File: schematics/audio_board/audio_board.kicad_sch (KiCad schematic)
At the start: 52 parts, among them J1 servo ctrl, J10 charge en, J3 power, J4 pyr ctrl, J5 servo out, J6 pyr in, J7 audio ctrl, J8 speaker, J9 battery, U1 TPS613222ADBV, U3 TPS613222ADBV, U4 TPS613222ADBV, U5 PAM8302AAD, U8 MCP73812

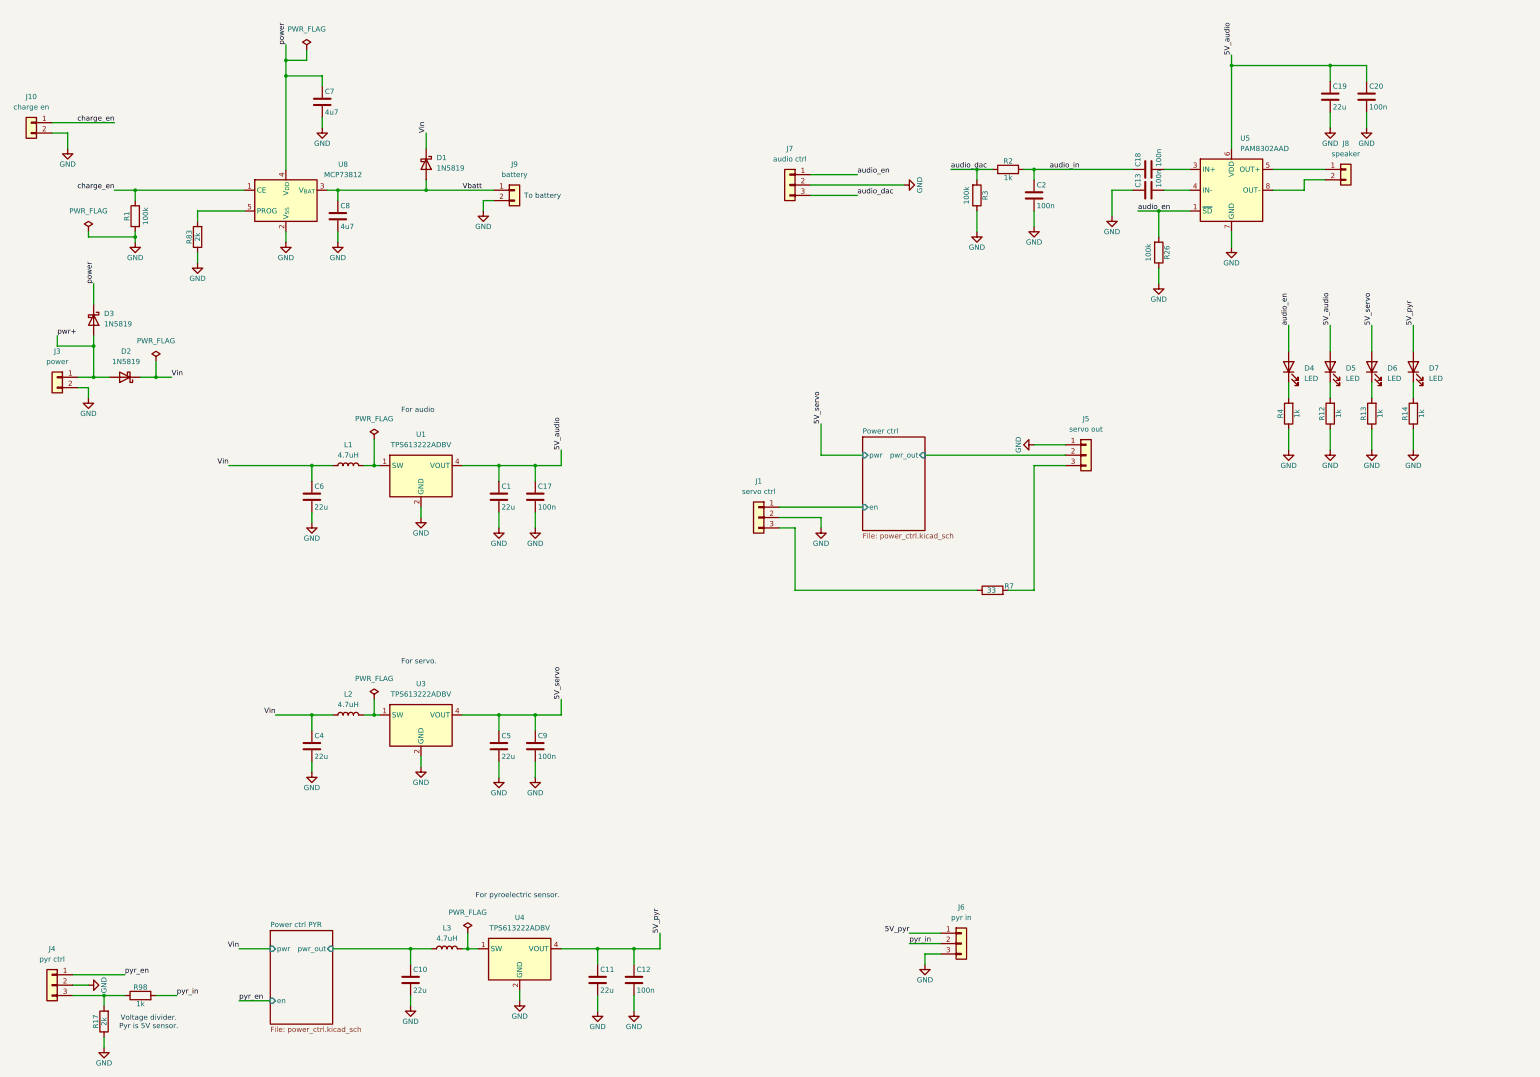
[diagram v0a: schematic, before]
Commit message: Redesigning audio board to support microphone.
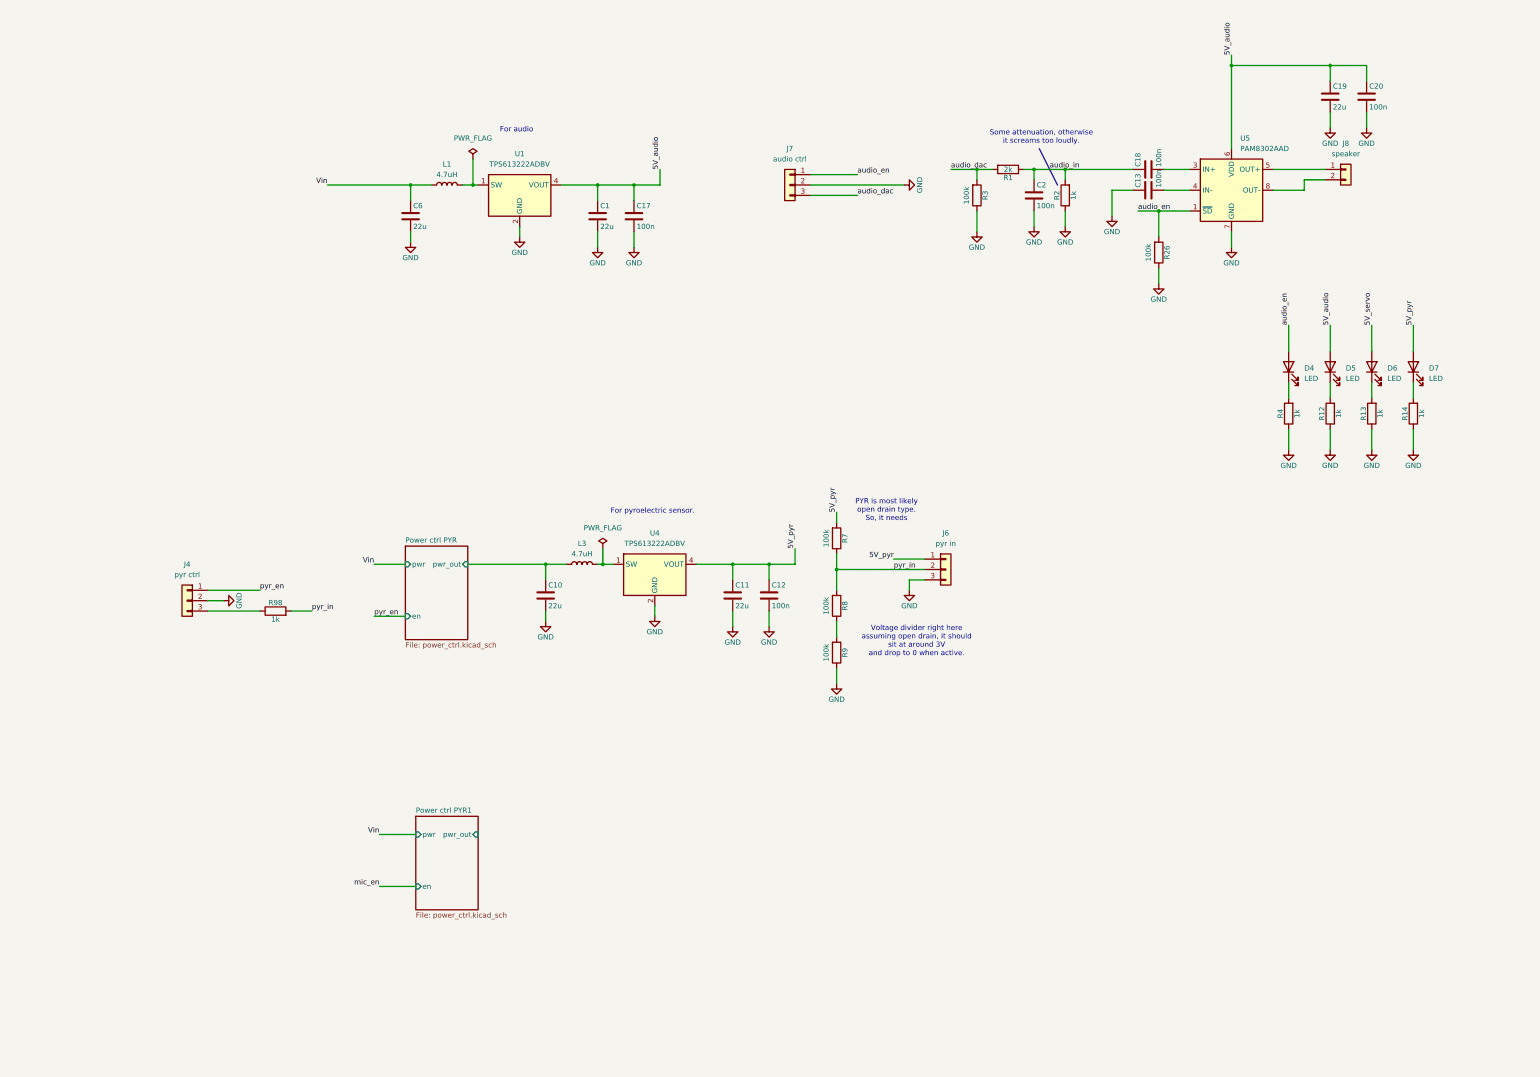
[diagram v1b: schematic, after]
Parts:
- removed C4, C5: 22u, Capacitor_SMD:C_0603_1608Metric_Pad1.08x0.95mm_HandSolder, symbol Device:C
- removed C7, C8: 4u7, Capacitor_SMD:C_0603_1608Metric_Pad1.08x0.95mm_HandSolder, symbol Device:C
- removed C9: 100n, Capacitor_SMD:C_0603_1608Metric_Pad1.08x0.95mm_HandSolder, symbol Device:C
- removed D1, D2, D3: 1N5819, Diode_THT:D_DO-41_SOD81_P7.62mm_Horizontal, symbol Device:D_Schottky
- removed J1: servo ctrl, Connector_PinSocket_2.54mm:PinSocket_1x03_P2.54mm_Vertical, symbol Connector_Generic:Conn_01x03
- removed J10: charge en, Connector_PinSocket_2.54mm:PinSocket_1x02_P2.54mm_Vertical, symbol Connector_Generic:Conn_01x02
- removed J3: power, Connector_PinSocket_2.54mm:PinSocket_1x02_P2.54mm_Vertical, symbol Connector_Generic:Conn_01x02
- removed J5: servo out, Connector_PinSocket_2.54mm:PinSocket_1x03_P2.54mm_Vertical, symbol Connector_Generic:Conn_01x03
- removed J9: battery, Connector_PinSocket_2.54mm:PinSocket_1x02_P2.54mm_Vertical, symbol Connector_Generic:Conn_01x02
- removed L2: 4.7uH, Inductor_SMD:L_1008_2520Metric, symbol Device:L
- removed R17, R83: 2k, Capacitor_SMD:C_0603_1608Metric_Pad1.08x0.95mm_HandSolder, symbol Device:R
- removed U3: TPS613222ADBV, Package_TO_SOT_SMD:SOT-23-5, symbol Regulator_Switching:TPS613222ADBV
- removed U8: MCP73812, Package_TO_SOT_SMD:SOT-23-5, symbol Battery_Management:MCP73812T-420I-OT
- added R8, R9: 100k, Resistor_SMD:R_0603_1608Metric_Pad0.98x0.95mm_HandSolder, symbol Device:R
- R1: value 100k -> 2k; footprint Resistor_SMD:R_0603_1608Metric_Pad0.98x0.95mm_HandSolder -> Capacitor_SMD:C_0603_1608Metric_Pad1.08x0.95mm_HandSolder; URL (none) -> https://www.digikey.com/en/products/detail/yageo/AC0603JR-0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
- R7: value 33 -> 100k
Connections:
- net charge_en is gone; now on net audio_in: R1.1
- net 5V_pyr: now also R7.2
- net GND: now also R2.1, R9.1; no longer R1.2
- net audio_dac: now also R1.2; no longer R2.1
- net pyr_in: now also R7.1, R8.2
- new net: R8.1, R9.2
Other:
- removed sheet Power ctrl
- added sheet Power ctrl PYR1 (power_ctrl.kicad_sch)
- note added: "PYR is most likely open drain type. So, it needs"
- note added: "Some attenuation, otherwise it screams too loudly."
- note added: "Voltage divider right here assuming open drain, it should sit at around 3V and drop to 0 when active."
- note removed: "For servo."
- note removed: "To battery"
- note removed: "Voltage divider. Pyr is 5V sensor."
- moved on the sheet: C1, C10, C11, C12, C17, C6, J4, J6, L1, L3, R2, R98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

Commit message: Replaced thick film with thin film resistors in feedback loops.
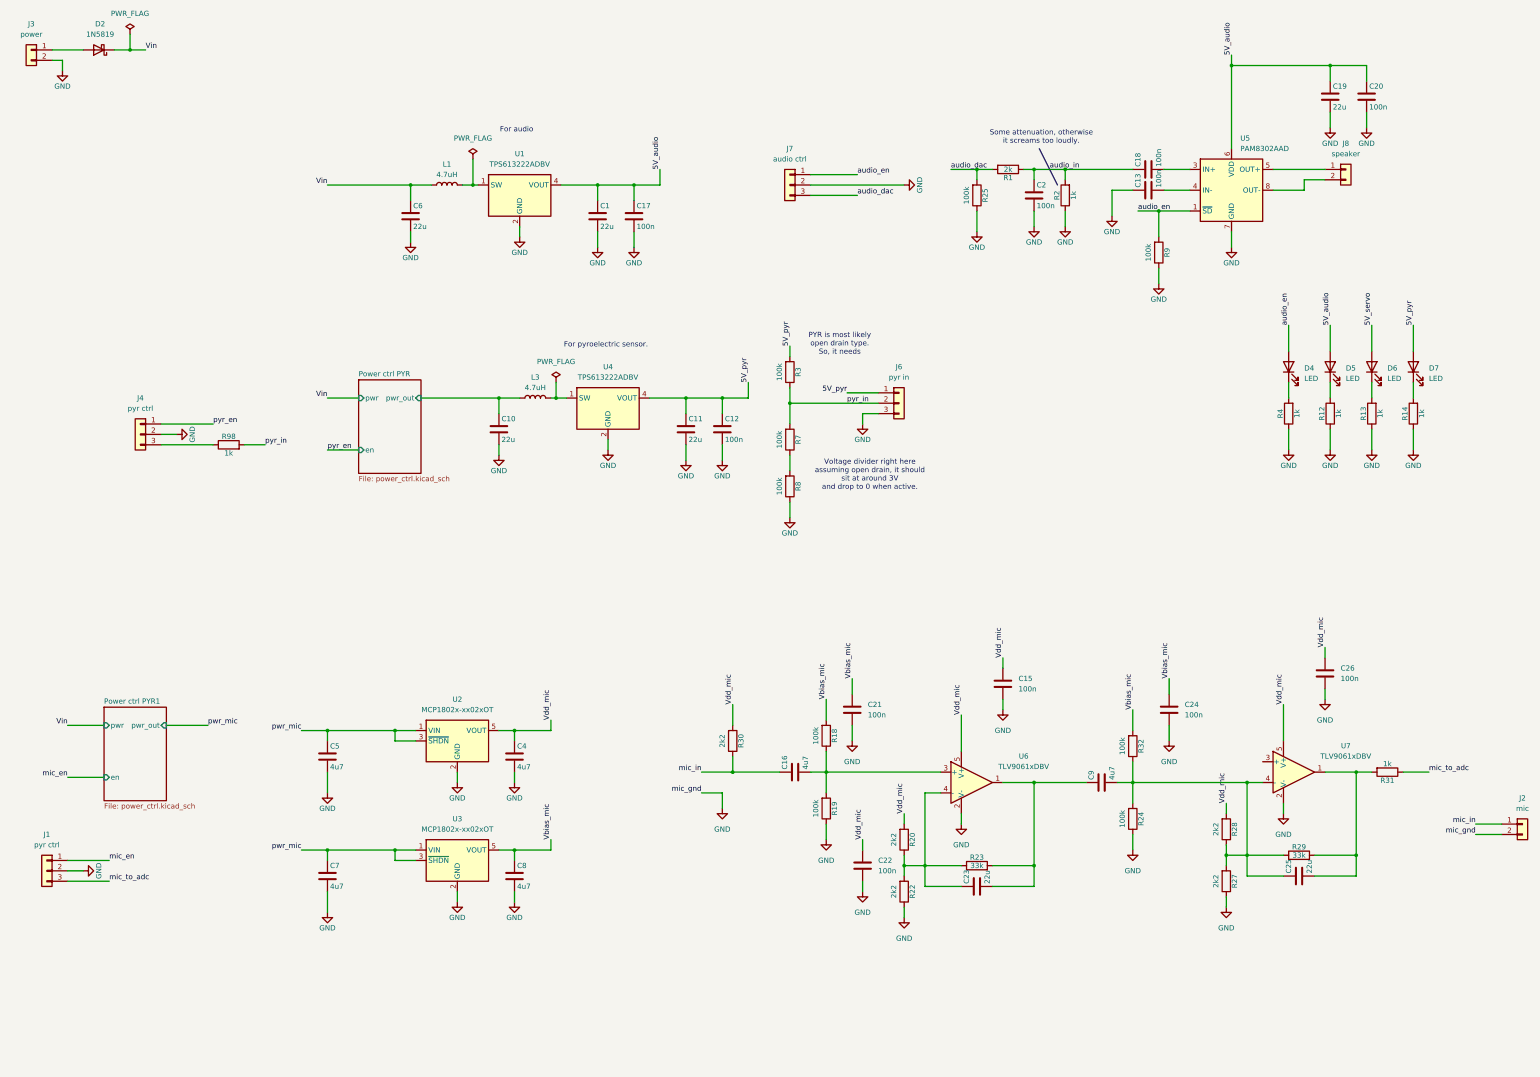
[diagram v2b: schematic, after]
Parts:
- removed R26: 100k, Resistor_SMD:R_0603_1608Metric_Pad0.98x0.95mm_HandSolder, symbol Device:R
- added C15, C21, C22, C24, C26: 100n, Capacitor_SMD:C_0603_1608Metric, symbol Device:C
- added C16, C4, C5, C7, C8, C9: 4u7, Capacitor_SMD:C_0603_1608Metric, symbol Device:C
- added C23, C25: 22u, Capacitor_SMD:C_0603_1608Metric_Pad1.08x0.95mm_HandSolder, symbol Device:C
- added D2: 1N5819, Diode_THT:D_DO-41_SOD81_P7.62mm_Horizontal, symbol Device:D_Schottky
- added J1: pyr ctrl, Connector_PinSocket_2.54mm:PinSocket_1x03_P2.54mm_Vertical, symbol Connector_Generic:Conn_01x03
- added J2: mic, Connector_PinSocket_2.54mm:PinSocket_1x02_P2.54mm_Vertical, symbol Connector_Generic:Conn_01x02
- added J3: power, Connector_PinSocket_2.54mm:PinSocket_1x02_P2.54mm_Vertical, symbol Connector_Generic:Conn_01x02
- added R18, R19, R24, R25, R32: 100k, Resistor_SMD:R_0603_1608Metric_Pad0.98x0.95mm_HandSolder, symbol Device:R
- added R20, R22, R27, R28, R30: 2k2, Resistor_SMD:R_0603_1608Metric_Pad0.98x0.95mm_HandSolder, symbol Device:R
- added R23, R29: 33k, Capacitor_SMD:C_0603_1608Metric_Pad1.08x0.95mm_HandSolder, symbol Device:R
- added R31: 1k, Capacitor_SMD:C_0603_1608Metric_Pad1.08x0.95mm_HandSolder, symbol Device:R
- added U2, U3: MCP1802x-xx02xOT, Package_TO_SOT_SMD:SOT-23-5, symbol Regulator_Linear:MCP1802x-xx02xOT
- added U6, U7: TLV9061xDBV, Package_TO_SOT_SMD:SOT-23-5, symbol Amplifier_Operational:TLV9061xDBV
- R3, R7, R8, R9: url (none) -> https://www.digikey.com/en/products/detail/susumu/RG1608P-1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
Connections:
- net 5V_pyr: now also R3.2; no longer R7.2
- net GND: now also R8.1, C15.2, C21.2, C22.2, C24.2, C26.2, C4.2, C5.2, C7.2, C8.2, J1.2 (Pin_2), J2.2 (Pin_2), J3.2 (Pin_2), R19.1, R22.1, R24.1, R25.1, R27.1, U2.2 (GND), U3.2 (GND), U6.2 (V-), U7.2 (V-); no longer R3.1
- net Vin: now also D2.1 (K)
- net audio_dac: now also R25.2; no longer R3.2
- net audio_en: now also R9.2
- net mic_en: now also J1.1 (Pin_1)
- net pyr_in: now also R3.1, R7.2; no longer R7.1, R8.2
- new net: R7.1, R8.2
- new net: C25.2, R29.2, R31.2, U7.1
- new net: C23.2, C9.1, R23.2, U6.1
- new net: C16.2, R18.1, R19.2, U6.3 (+)
- new net: C23.1, R20.1, R22.2, R23.1, U6.4 (-)
- new net: C25.1, C9.2, R24.2, R27.2, R28.1, R29.1, R32.1, U7.4 (-)
- new net: D2.2 (A), J3.1 (Pin_1)
- new net Vbias_mic: C21.1, C24.1, C8.1, R18.2, R32.2, U3.5 (VOUT)
- new net Vdd_mic: C15.1, C22.1, C26.1, C4.1, R20.2, R28.2, R30.2, U2.5 (VOUT), U6.5 (V+), U7.5 (V+)
- new net mic_in: C16.1, J2.1 (Pin_1), R30.1
- new net mic_to_adc: J1.3 (Pin_3), R31.1
- new net pwr_mic: C5.1, C7.1, U2.1 (VIN), U2.3 (~{SHDN}), U3.1 (VIN), U3.3 (~{SHDN})
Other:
- moved on the sheet: C10, C11, C12, J4, J6, L3, R98, U4

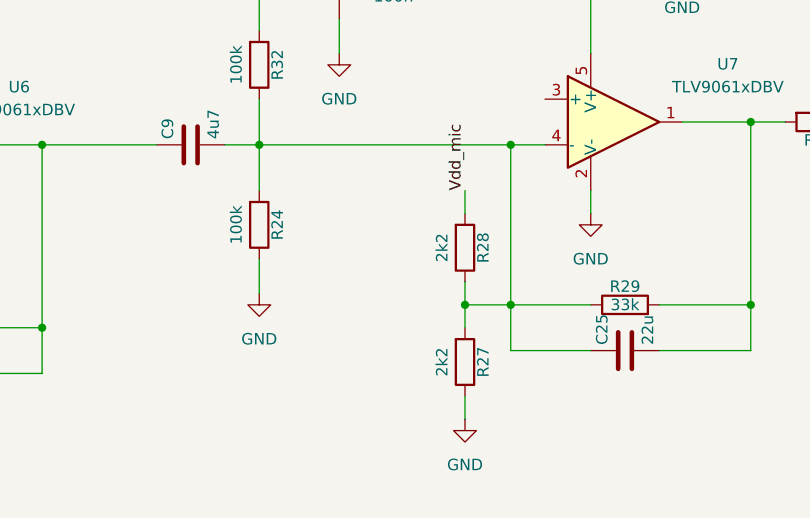
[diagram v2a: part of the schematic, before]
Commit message: Added filtering capacitor.
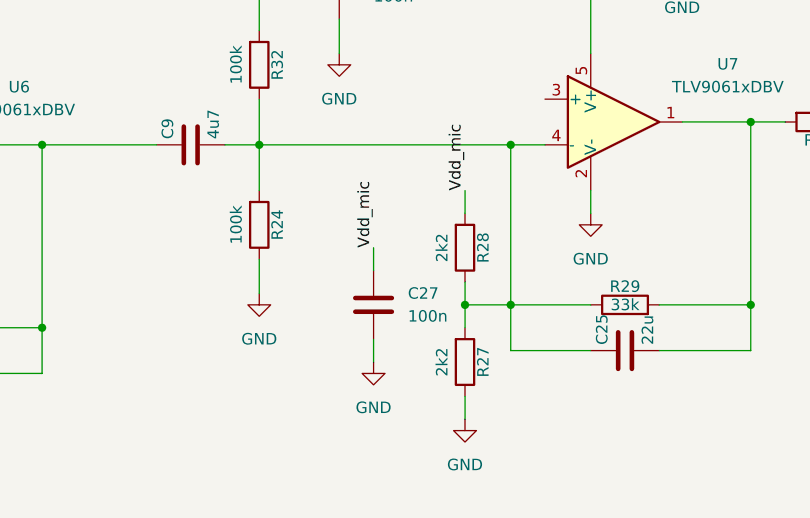
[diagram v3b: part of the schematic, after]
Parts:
- added C27: 100n, Capacitor_SMD:C_0603_1608Metric, symbol Device:C
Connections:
- net GND: now also C27.2
- net Vdd_mic: now also C27.1
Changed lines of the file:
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@@
 	(wire
 		(pts
+			(xy 306.07 214.63) (xy 306.07 217.17)
+		)
+		(stroke
+			(width 0)
+			(type default)
+		)
+	)
+	(wire
+		(pts
 			(xy 341.63 39.37) (xy 341.63 43.18)
 		)
@@
 	(wire
 		(pts
+			(xy 306.07 224.79) (xy 306.07 227.33)
+		)
+		(stroke
+			(width 0)
+			(type default)
+		)
+	)
+	(wire
+		(pts
 			(xy 289.56 203.2) (xy 293.37 203.2)
 		)
@@
 		)
 	)
+	(label "Vdd_mic"
+		(at 306.07 214.63 90)
+		(effects
+			(font
+				(size 1.27 1.27)
+			)
+			(justify left bottom)
+		)
+	)
 	(label "mic_in"
 		(at 187.96 200.66 180)
@@
 	(symbol
 		(lib_id "Device:C")
+		(at 306.07 220.98 0)
+		(unit 1)
+		(exclude_from_sim no)
+		(in_bom yes)
+		(on_board yes)
+		(dnp no)
+		(fields_autoplaced yes)
+		(property "Reference" "C27"
+			(at 309.88 219.7099 0)
+			(effects
+				(font
+					(size 1.27 1.27)
+				)
+				(justify left)
+			)
+		)
+		(property "Value" "100n"
+			(at 309.88 222.2499 0)
+			(effects
+				(font
+					(size 1.27 1.27)
+				)
+				(justify left)
+			)
+		)
+		(property "Footprint" "Capacitor_SMD:C_0603_1608Metric"
+			(at 307.0352 224.79 0)
+			(effects
+				(font
+					(size 1.27 1.27)
+				)
+				(hide yes)
+			)
+		)
+		(property "Datasheet" "~"
+			(at 306.07 220.98 0)
+			(effects
+				(font
+					(size 1.27 1.27)
+				)
+				(hide yes)
+			)
+		)
+		(property "Description" "Unpolarized capacitor"
+			(at 306.07 220.98 0)
+			(effects
+				(font
+					(size 1.27 1.27)
+				)
+				(hide yes)
+			)
+		)
+		(property "url" "https://www.digikey.com/en/products/detail/yageo/CC0603KRX7R7BB104/302822"
+			(at 306.07 220.98 0)
+			(effects
+				(font
+					(size 1.27 1.27)
+				)
+				(hide yes)
+			)
+		)
+		(pin "1"
+		)
+		(pin "2"
+		)
+		(instances
+			(project "audio_board"
+				(path "/baedfaab-6940-4c04-b4a7-304f9ffa239d"
+					(reference "C27")
+					(unit 1)
+				)
+			)
+		)
+	)
+	(symbol
+		(lib_id "Device:C")
 		(at 224.79 185.42 0)
 		(unit 1)
@@
 					(unit 1)
 				)
+			)
+		)
+	)
+	(symbol
+		(lib_id "power:GND")
+		(at 306.07 227.33 0)
+		(unit 1)
+		(exclude_from_sim no)
+		(in_bom yes)
+		(on_board yes)
+		(dnp no)
+		(fields_autoplaced yes)
+		(property "Reference" "#PWR051"
+			(at 306.07 233.68 0)
+			(effects
+				(font
+					(size 1.27 1.27)
+				)
+				(hide yes)
+			)
+		)
+		(property "Value" "GND"
+			(at 306.07 232.41 0)
+			(effects
+				(font
+					(size 1.27 1.27)
+				)
+			)
+		)
+		(property "Footprint" ""
+			(at 306.07 227.33 0)
+			(effects
+				(font
+					(size 1.27 1.27)
+				)
+				(hide yes)
+			)
+		)
+		(property "Datasheet" ""
+			(at 306.07 227.33 0)
+			(effects
+				(font
+					(size 1.27 1.27)
+				)
+				(hide yes)
+			)
+		)
+		(property "Description" "Power symbol creates a global label with name \"GND\" , ground"
+			(at 306.07 227.33 0)
+			(effects
+				(font
+					(size 1.27 1.27)
+				)
+				(hide yes)
+			)
+		)
+		(pin "1"
+		)
+		(instances
+			(project "audio_board"
+				(path "/baedfaab-6940-4c04-b4a7-304f9ffa239d"
+					(reference "#PWR051")
+					(unit 1)
+				)
